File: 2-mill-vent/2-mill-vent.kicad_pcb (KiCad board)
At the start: 2 copper layers, 96.5 x 55.9 mm, 56 parts, among them J1 Differential:/Single, J3 No_Power_Control, J4 Front_panel_control, J5 Fan, J6 Ext Parts, J7 EXT Power Option, J8 POWER, Q1 2N3904, Q2 2N3904, Q3 2N3904, Q4 TSM480P06CHX0G-Transistor_FET, U1 LM358, U2 LM78L05_TO92, U3 TSR_1-24120, U4 MPXV

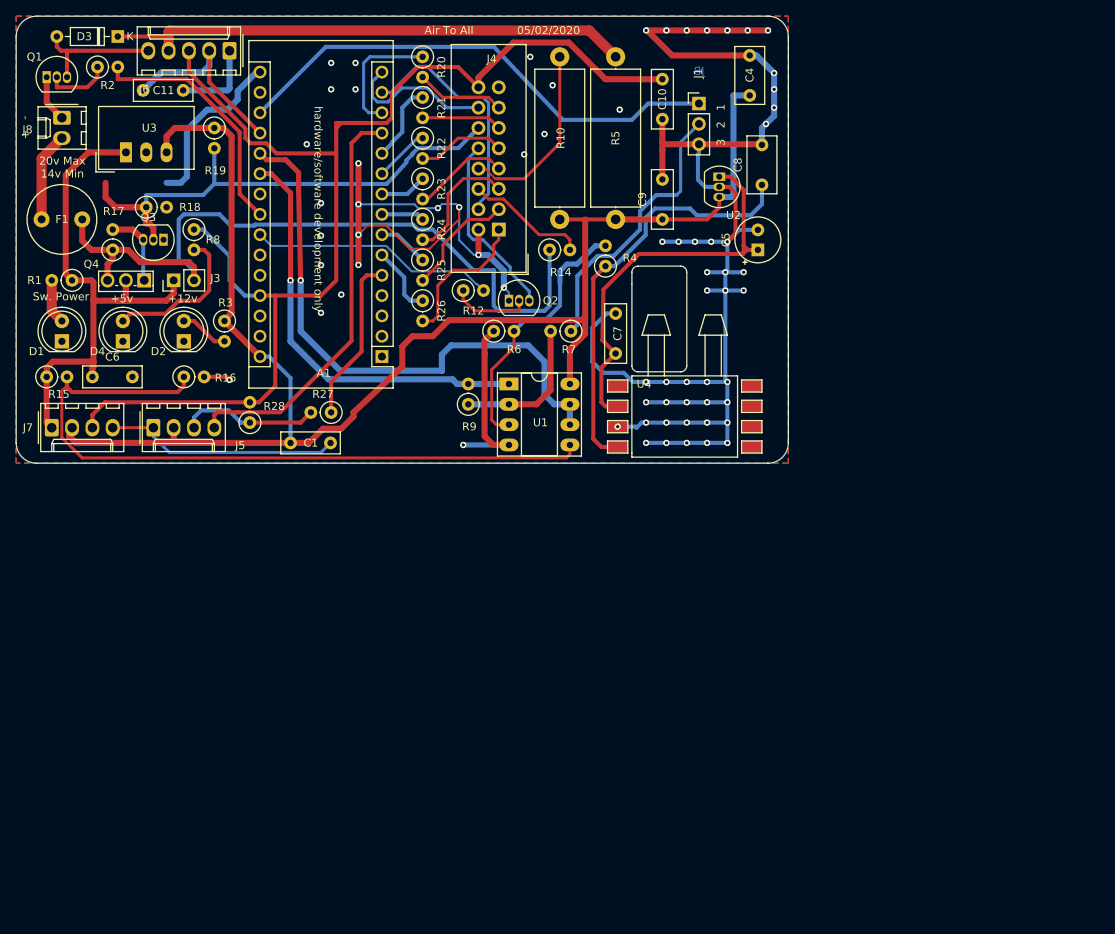
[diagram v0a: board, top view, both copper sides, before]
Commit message: Made major changes to 2A and started an all in one board
2A is a longer SMD front panel board now, no plans on updating 2b. work on 1, 2 , 2A, 2B has stoped.
Now looking at 3 to cut cost greatly with not having to interconnect two boards and make two boards. just the parts cost savings is in the order of $30 in qty1
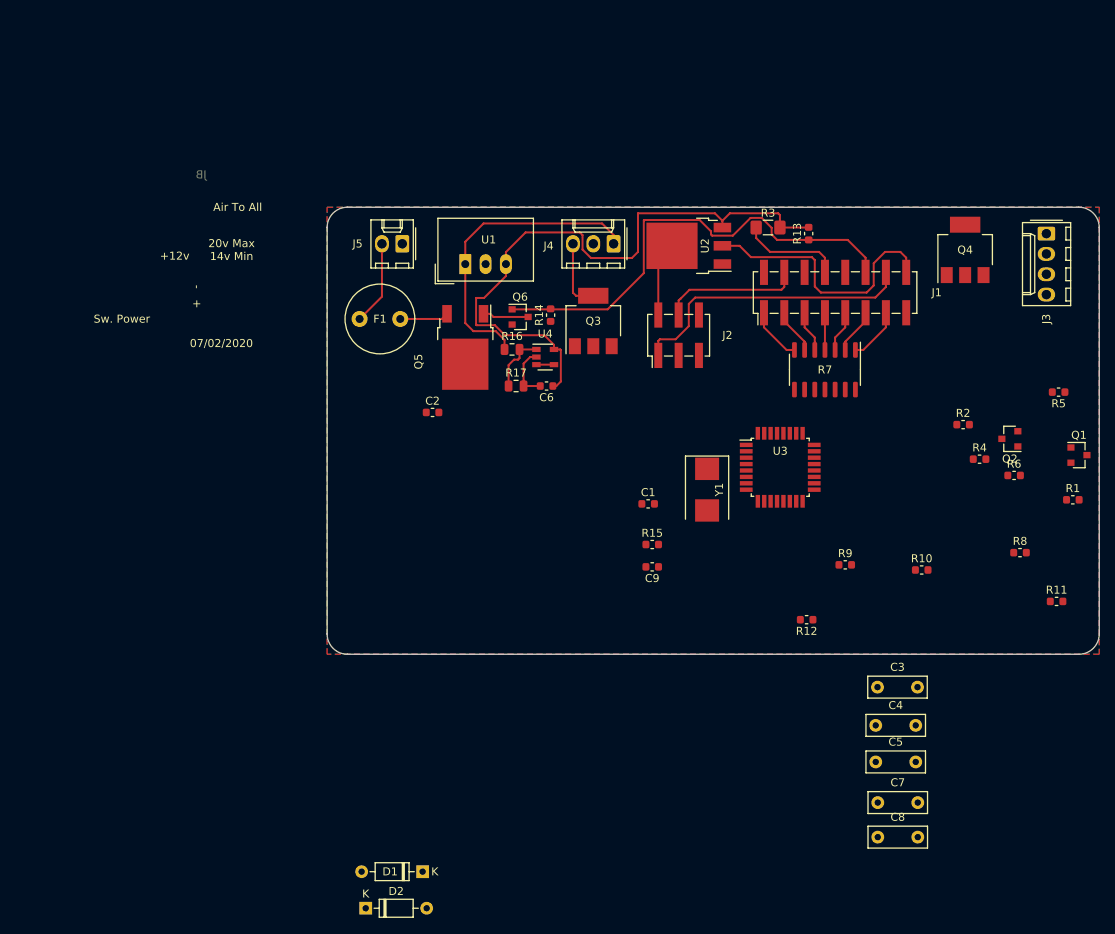
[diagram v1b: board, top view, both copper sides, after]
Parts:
- removed A1: Arduino_Nano_v3.x, Module:Arduino_Nano
- removed C10, C11: 0.1uF, Capacitor_THT:C_Rect_L7.2mm_W2.5mm_P5.00mm_FKS2_FKP2_MKS2_MKP2
- removed the C9 at (172.2, 91.4)
- removed the D1 at (97.2, 106.7)
- removed D4: +5V, LED_THT:LED_D5.0mm
- removed the J1 at (176.8, 77.0)
- removed the J3 at (111.1, 99.1)
- removed J6: Ext Parts, Connector_Molex:Molex_KK-254_AE-6410-05A_1x05_P2.54mm_Vertical
- removed J7: EXT Power Option, Connector_Molex:Molex_KK-254_AE-6410-04A_1x04_P2.54mm_Vertical
- removed R18: 1m, Resistor_THT:R_Axial_DIN0207_L6.3mm_D2.5mm_P2.54mm_Vertical
- removed R20, R21, R22, R23, R24, R25, R26: 330, Resistor_THT:R_Axial_DIN0207_L6.3mm_D2.5mm_P2.54mm_Vertical
- removed R28: 10k, Resistor_THT:R_Axial_DIN0207_L6.3mm_D2.5mm_P2.54mm_Vertical
- removed the R3 at (117.5, 104.1)
- removed the R8 at (113.7, 92.7)
- removed the R9 at (148.0, 114.6)
- removed the U1 at (153.0, 112.0)
- added C1: C0603C104M4RACTU, Capacitor_SMD:C_0603_1608Metric, F.Cu at (170.4, 127.0)
- added C3: 1uF, Capacitor_THT:C_Rect_L7.2mm_W2.5mm_P5.00mm_FKS2_FKP2_MKS2_MKP2, F.Cu at (199.1, 149.9)
- added C6: C0603C104M4RACTU, Capacitor_SMD:C_0603_1608Metric, F.Cu at (157.7, 112.3)
- added J2: ICSP, Connector_PinHeader_2.54mm:PinHeader_2x03_P2.54mm_Vertical_SMD, F.Cu at (174.2, 105.9)
- added J4: Buzzer, Connector_Molex:Molex_KK-254_AE-6410-03A_1x03_P2.54mm_Vertical, F.Cu at (166.1, 94.5)
- added Q4: PZT3904, Package_TO_SOT_SMD:SOT-223-3_TabPin2, F.Cu at (210.1, 95.2)
- added Q6: MMBT3904, Package_TO_SOT_SMD:SOT-23, F.Cu at (154.4, 103.6)
- added R14: 1M, Resistor_SMD:R_0603_1608Metric, F.Cu at (158.2, 103.4)
- added R15: 10k, Resistor_SMD:R_0603_1608Metric, F.Cu at (170.9, 132.1)
- added R2: 10k, Resistor_SMD:R_0603_1608Metric, F.Cu at (209.8, 117.1)
- added U3: ATmega328P-AU, Package_QFP:TQFP-32_7x7mm_P0.8mm, F.Cu at (186.9, 122.4)
- added Y1: ABLS7M-16.000MHZ-B-2-T, Crystal:Crystal_SMD_7050-2Pin_7.0x5.0mm, F.Cu at (177.8, 125.2)
- C2: renamed from C6; value 0.1uF -> C0603C104M4RACTU; footprint Capacitor_THT:C_Rect_L7.2mm_W2.5mm_P5.00mm_FKS2_FKP2_MKS2_MKP2 -> Capacitor_SMD:C_0603_1608Metric
- C4: value 10uF -> 1uF; footprint Capacitor_THT:C_Rect_L7.0mm_W3.5mm_P5.00mm -> Capacitor_THT:C_Rect_L7.2mm_W2.5mm_P5.00mm_FKS2_FKP2_MKS2_MKP2
- C5: footprint Capacitor_THT:CP_Radial_Tantal_D5.5mm_P2.50mm -> Capacitor_THT:C_Rect_L7.2mm_W2.5mm_P5.00mm_FKS2_FKP2_MKS2_MKP2
- C7: value 0.1uF -> 10uF
- C8: value 470pF -> 1uF; footprint Capacitor_THT:C_Rect_L7.0mm_W3.5mm_P5.00mm -> Capacitor_THT:C_Rect_L7.2mm_W2.5mm_P5.00mm_FKS2_FKP2_MKS2_MKP2
- C9: renamed from C1; value 0.1uF -> C0603C104M4RACTU; footprint Capacitor_THT:C_Rect_L7.2mm_W2.5mm_P5.00mm_FKS2_FKP2_MKS2_MKP2 -> Capacitor_SMD:C_0603_1608Metric
- D2: value +12V -> 1N914; footprint LED_THT:LED_D5.0mm -> Diode_THT:D_DO-35_SOD27_P7.62mm_Horizontal
- J1: renamed from J4; value Front_panel_control -> 71349-1006; footprint Connector_IDC:IDC-Header_2x08_P2.54mm_Vertical -> Connector_PinHeader_2.54mm:PinHeader_2x08_P2.54mm_Vertical_SMD
- Q1, Q2: value 2N3904 -> MMBT3904; footprint Package_TO_SOT_THT:TO-92_Inline -> Package_TO_SOT_SMD:SOT-23
- Q3: value 2N3904 -> PZT3904; footprint Package_TO_SOT_THT:TO-92_Inline -> Package_TO_SOT_SMD:SOT-223-3_TabPin2
- Q5: renamed from Q4; value TSM480P06CHX0G-Transistor_FET -> TSM480P06CP; footprint Package_TO_SOT_THT:TO-251-3_Vertical -> Package_TO_SOT_SMD:TO-252-2
- R1: value 1.8k -> 10k; footprint Resistor_THT:R_Axial_DIN0207_L6.3mm_D2.5mm_P2.54mm_Vertical -> Resistor_SMD:R_0603_1608Metric
- R10: value 110 1W -> 10k; footprint Resistor_THT:R_Axial_DIN0617_L17.0mm_D6.0mm_P20.32mm_Horizontal -> Resistor_SMD:R_0603_1608Metric
- R11: renamed from R14; footprint Resistor_THT:R_Axial_DIN0207_L6.3mm_D2.5mm_P2.54mm_Vertical -> Resistor_SMD:R_0603_1608Metric
- R12: renamed from R17; footprint Resistor_THT:R_Axial_DIN0207_L6.3mm_D2.5mm_P2.54mm_Vertical -> Resistor_SMD:R_0603_1608Metric
- R13: renamed from R19; footprint Resistor_THT:R_Axial_DIN0207_L6.3mm_D2.5mm_P2.54mm_Vertical -> Resistor_SMD:R_0603_1608Metric
- R16: renamed from R15; value 33k -> RN73H2ATTD3302D25; footprint Resistor_THT:R_Axial_DIN0207_L6.3mm_D2.5mm_P2.54mm_Vertical -> Resistor_SMD:R_0805_2012Metric
- R17: renamed from R16; value 8.2k -> RN73H2ATTD8201F25; footprint Resistor_THT:R_Axial_DIN0207_L6.3mm_D2.5mm_P2.54mm_Vertical -> Resistor_SMD:R_0805_2012Metric
- R3: renamed from R5; value 300 1/2W -> LTR18EZPJ301; footprint Resistor_THT:R_Axial_DIN0617_L17.0mm_D6.0mm_P20.32mm_Horizontal -> Resistor_SMD:R_1206_3216Metric_Pad1.42x1.75mm_HandSolder
- R4: value 10k -> 330; footprint Resistor_THT:R_Axial_DIN0207_L6.3mm_D2.5mm_P2.54mm_Vertical -> Resistor_SMD:R_0603_1608Metric
- R5: renamed from R27; value 1k -> 10k; footprint Resistor_THT:R_Axial_DIN0207_L6.3mm_D2.5mm_P2.54mm_Vertical -> Resistor_SMD:R_0603_1608Metric
- R6: value 10k -> 1k; footprint Resistor_THT:R_Axial_DIN0207_L6.3mm_D2.5mm_P2.54mm_Vertical -> Resistor_SMD:R_0603_1608Metric
- R7: value 5k -> 4814P-1-331LF; footprint Resistor_THT:R_Axial_DIN0207_L6.3mm_D2.5mm_P2.54mm_Vertical -> Package_SO:SOIC-14_3.9x8.7mm_P1.27mm
- R8: renamed from R12; footprint Resistor_THT:R_Axial_DIN0207_L6.3mm_D2.5mm_P2.54mm_Vertical -> Resistor_SMD:R_0603_1608Metric
- R9: renamed from R2; footprint Resistor_THT:R_Axial_DIN0207_L6.3mm_D2.5mm_P2.54mm_Vertical -> Resistor_SMD:R_0603_1608Metric
- U2: value LM78L05_TO92 -> LM1117-5.0; footprint Package_TO_SOT_THT:TO-92_Inline -> Package_TO_SOT_SMD:TO-252-3_TabPin2
- U4: value MPXV -> LM321; footprint Sensor:MPXV -> Package_TO_SOT_SMD:SOT-23-5
- moved Q1 137.4 mm to (224.3, 120.9)
- moved R1 128.1 mm to (223.5, 126.5), turned to 0 degrees
- moved J3 114.2 mm to (220.2, 93.2), turned to 270 degrees
- moved R9 112.3 mm to (195.1, 134.6)
- moved D1 111.1 mm to (142.2, 173.0)
- moved R12 98.3 mm to (190.2, 141.5), turned to 180 degrees
- moved R5 91.0 mm to (221.7, 113.0)
- moved C8 82.8 mm to (199.1, 168.7), turned to 0 degrees
- moved C4 80.3 mm to (198.9, 154.7), turned to 0 degrees
- moved R10 78.5 mm to (204.6, 135.3), turned to 0 degrees
- moved R11 77.1 mm to (221.5, 139.2)
- moved R8 76.9 mm to (216.9, 133.1)
- moved R13 75.5 mm to (190.5, 93.2), turned to 90 degrees
- moved D2 74.4 mm to (135.1, 177.5), turned to 0 degrees
- moved R6 67.5 mm to (216.2, 123.4)
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- renumbered D3 to D1, J5 to J3, J8 to J5, U3 to U1
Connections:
- C4 pad 1: +12V -> Net-(C4-Pad1)
- C5 pad 1: Sensor_Power -> +12V
- C7 pad 1: Sensor_Power -> +5V
- C8 pad 1: Pressure -> ON\*OFF
- D1 pad 1: Motor+ -> SW_Batt
- D1 pad 2: Motor- -> Buzzer-
- D2 pad 1: GND -> Power_off
- D2 pad 2: Net-(D2-Pad2) -> Monitor
- J1 pad 1: Net-(J4-Pad1) -> Net-(J1-Pad1)
- J1 pad 10: Buzzer- -> Motor-
- J1 pad 11: Net-(J4-Pad11) -> Net-(J1-Pad11)
- J1 pad 13: Net-(J4-Pad13) -> Net-(J1-Pad13)
- J1 pad 3: Net-(J4-Pad3) -> Net-(J1-Pad3)
- J1 pad 5: Net-(J4-Pad5) -> Net-(J1-Pad5)
- J1 pad 7: Net-(J4-Pad7) -> Net-(J1-Pad7)
- J1 pad 8: Buzzer+ -> Motor+
- J1 pad 9: Net-(J4-Pad9) -> Net-(J1-Pad9)
- J3 pad 3: Net-(J5-Pad3) -> Raw_RPM
- J3 pad 4: PWM -> PWM_Drive
- Q1 pad 1: GND -> Net-(Q1-Pad1)
- Q1 pad 2: Net-(Q1-Pad2) -> GND
- Q1 pad 3: Motor- -> RPM
- Q2 pad 1: GND -> Net-(Q2-Pad1)
- Q2 pad 2: Net-(Q2-Pad2) -> GND
- Q2 pad 3: Buzzer- -> Net-(Q2-Pad3)
- Q3 pad 1: GND -> Net-(Q3-Pad1)
- Q3 pad 2: ON\*OFF -> Buzzer-
- Q3 pad 3: Net-(Q3-Pad3) -> GND
- Q5 pad 1: Net-(Q3-Pad3) -> Net-(Q5-Pad1)
- R1 pad 1: SW_Batt -> RPM
- R1 pad 2: Net-(D1-Pad2) -> +5V
- R10 pad 1: Buzzer+ -> Reset
- R10 pad 2: +12V -> +5V
- R12 pad 2: Net-(Q3-Pad3) -> Net-(Q5-Pad1)
- R13 pad 1: +12V -> ON\*OFF
- R13 pad 2: ON\*OFF -> +12V
- R16 pad 2: Net-(R15-Pad2) -> Net-(R16-Pad2)
- R17 pad 1: Net-(R15-Pad2) -> Net-(R16-Pad2)
- R4 pad 1: Pressure -> Net-(Q2-Pad3)
- R4 pad 2: Net-(R4-Pad2) -> PWM_Drive
- R5 pad 1: RPM -> Raw_RPM
- R5 pad 2: Net-(J5-Pad3) -> Net-(Q1-Pad1)
- R6 pad 1: GND -> PWM
- R6 pad 2: Net-(R4-Pad2) -> Net-(Q2-Pad1)
- R7 pad 1: Net-(J1-Pad2) -> Net-(J1-Pad13)
- R7 pad 2: Net-(R7-Pad2) -> Net-(J1-Pad11)
- R8 pad 1: Net-(Q2-Pad2) -> Net-(Q3-Pad1)
- R9 pad 1: Net-(Q1-Pad2) -> Net-(Q4-Pad1)
- U2 pad 1: Sensor_Power -> GND
- U2 pad 2: GND -> +5V
- U4 pad 1: Net-(U4-Pad1) -> Net-(R16-Pad2)
- U4 pad 2: Sensor_Power -> GND
- U4 pad 3: GND -> Batt_V
- U4 pad 4: Pressure -> Batt_V
- U4 pad 5: Net-(U4-Pad5) -> +12V
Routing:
- net GND: track 321.4 -> 6.83 mm, vias 68 -> 0
- net +5V: track 159.0 -> 42.6 mm
- net +12V: track 189.6 -> 78.2 mm
- net Net-(R15-Pad2): track 91.4 -> 0.00 mm
- net Raw_Batt: track 94.2 -> 6.11 mm
- net Batt_V: track 71.9 -> 2.20 mm, vias 1 -> 0
- net REF: track 63.1 -> 0.00 mm
- net Sensor_Power: track 59.7 -> 0.00 mm
- net Motor+: track 67.7 -> 12.8 mm
- net Pressure_V: track 52.9 -> 0.00 mm, vias 1 -> 0
- net Pressure: track 52.8 -> 0.00 mm
- net PWM: track 51.6 -> 0.00 mm
- net Net-(J1-Pad2): track 35.2 -> 0.00 mm
- net Net-(R4-Pad2): track 33.0 -> 0.00 mm
- net Motor: track 30.8 -> 0.00 mm
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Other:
- outline, holes or cut-outs redrawn
- board text added: "07/02/2020"
- board text removed: "+5v"
- board text removed: "05/02/2020"
- board text removed: "3 2 1"
- board text removed: "Batt Power In"
- board text removed: "Fan"
- board text removed: "Gnd +5v +12v Sw. Batt"
- board text removed: "Gnd SPD +5v Mot+ Mot-"
- board text removed: "PWM RPM +12v GND"
- board text removed: "Power Out"
- board text removed: "Pressure"
- board text removed: "Vacuum"
- board text removed: "hardware/software development only"
